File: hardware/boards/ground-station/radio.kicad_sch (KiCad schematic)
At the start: 0 parts

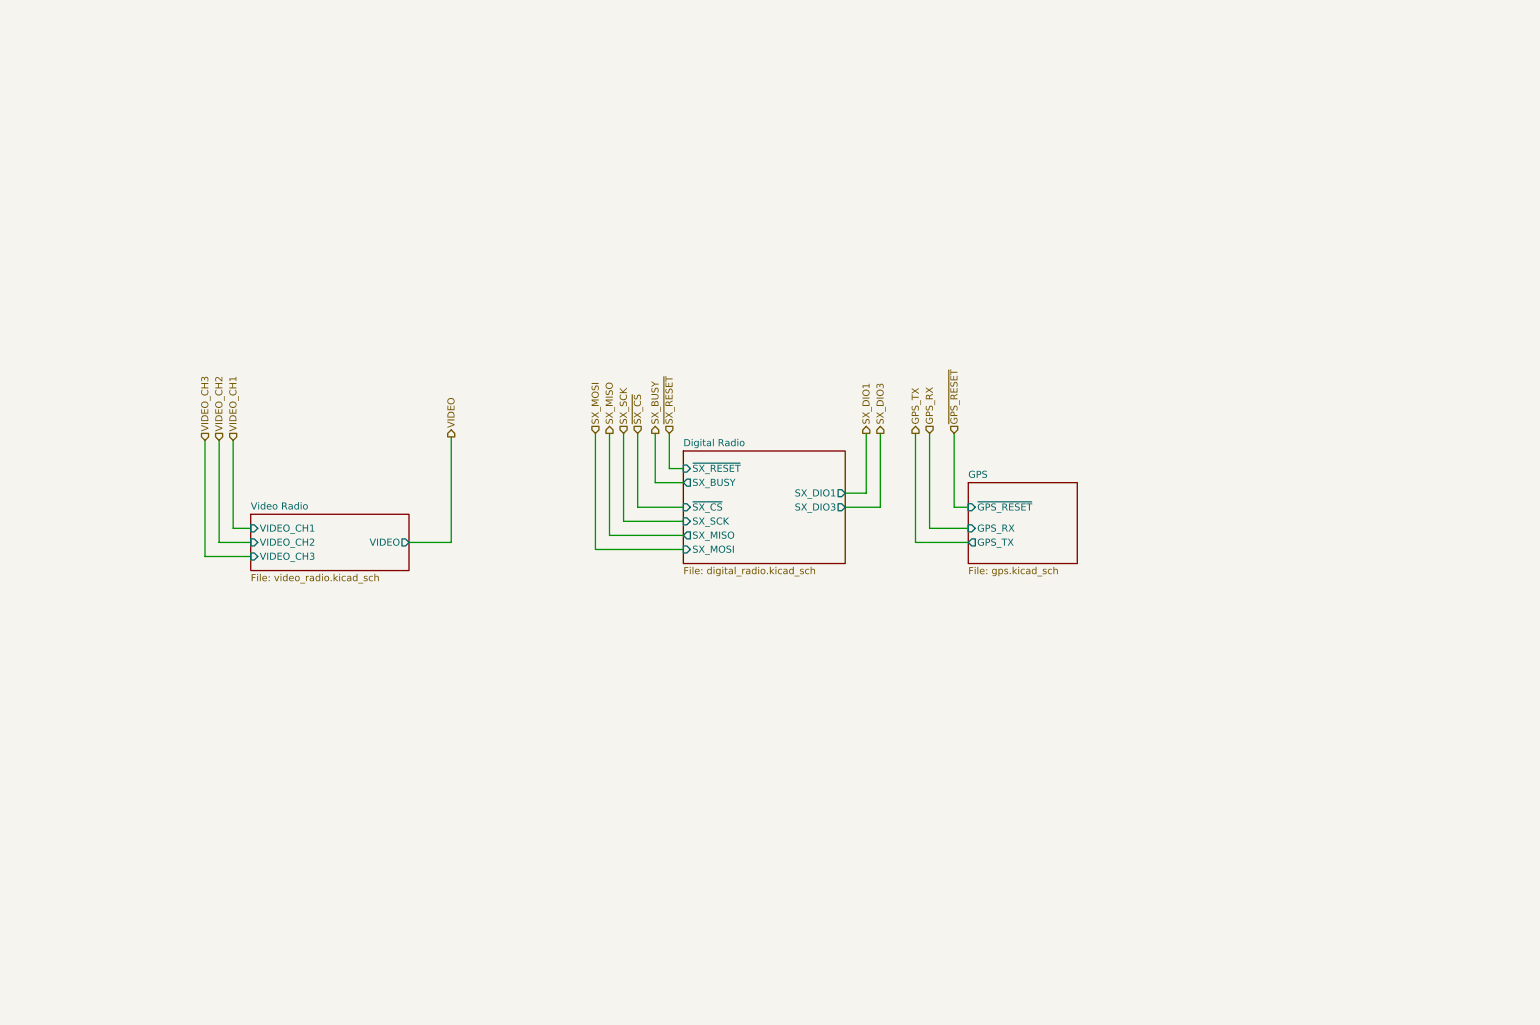
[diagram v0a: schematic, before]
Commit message: Updated video radio to RX5808
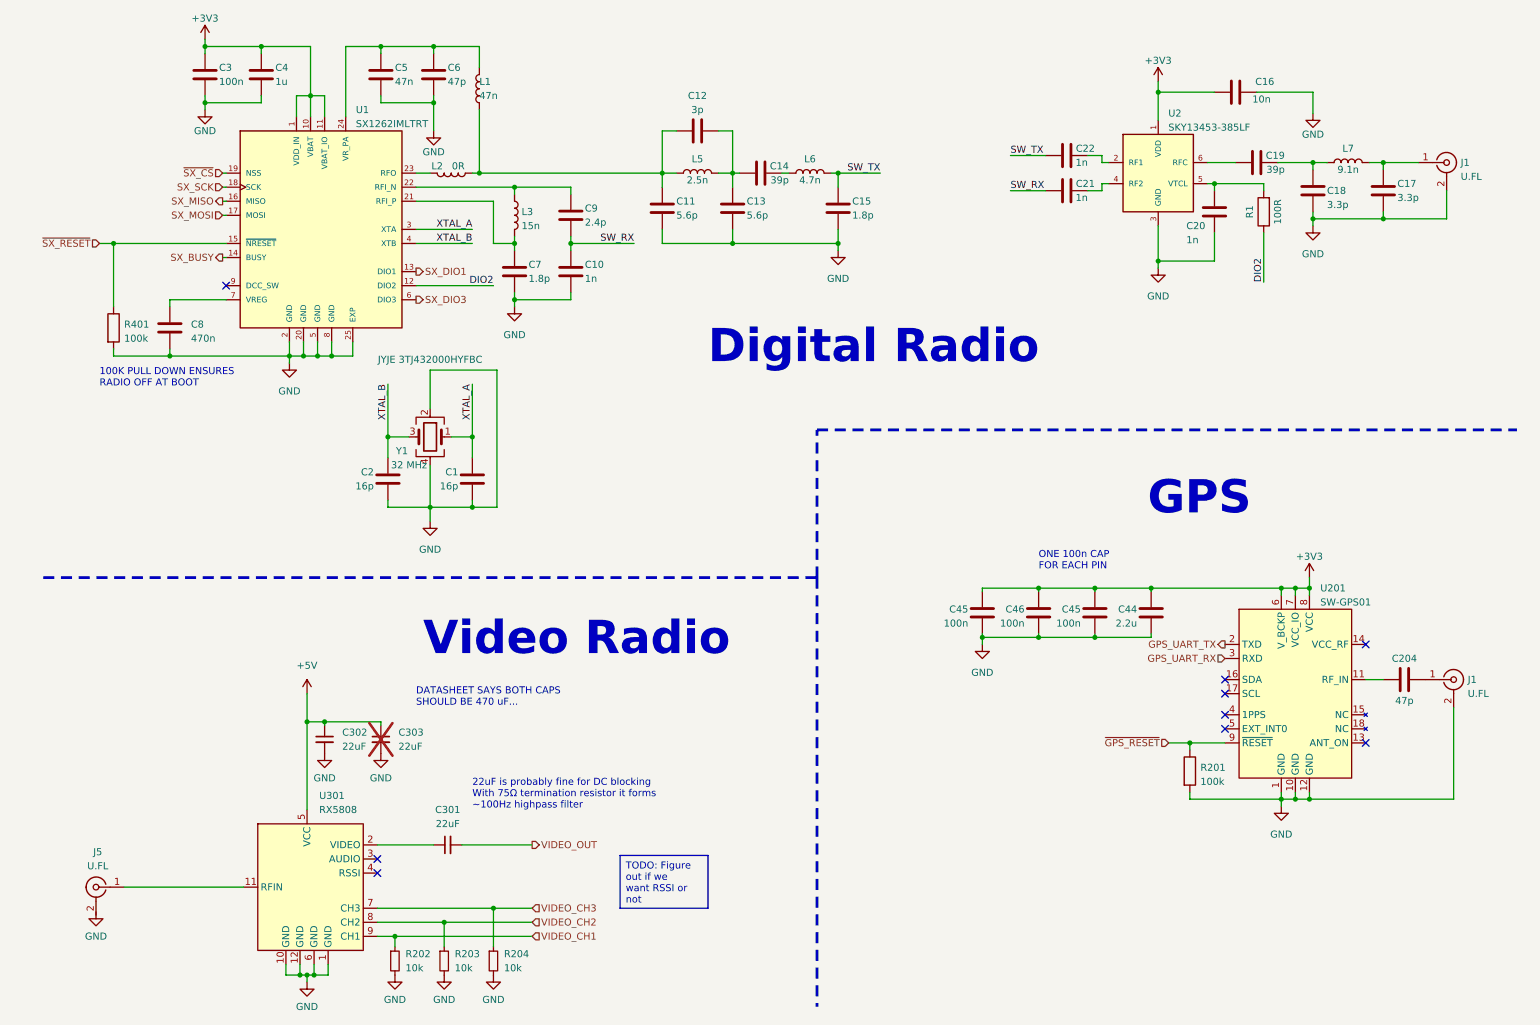
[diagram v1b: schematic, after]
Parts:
- added C1, C2: 16p, Capacitor_SMD:C_0201_0603Metric, symbol Device:C
- added C10, C21, C22: 1n, Capacitor_SMD:C_0402_1005Metric, symbol Device:C
- added C11, C13: 5.6p, Capacitor_SMD:C_0402_1005Metric, symbol Device:C
- added C12: 3p, Capacitor_SMD:C_0402_1005Metric, symbol Device:C
- added C14, C19: 39p, Capacitor_SMD:C_0402_1005Metric, symbol Device:C
- added C15, C7: 1.8p, Capacitor_SMD:C_0402_1005Metric, symbol Device:C
- added C16: 10n, Capacitor_SMD:C_0201_0603Metric, symbol Device:C
- added C17, C18: 3.3p, Capacitor_SMD:C_0402_1005Metric, symbol Device:C
- added C20: 1n, Capacitor_SMD:C_0201_0603Metric, symbol Device:C
- added C204, C6: 47p, Capacitor_SMD:C_0402_1005Metric, symbol Device:C
- added C3, C45 (x2), C46: 100n, Capacitor_SMD:C_0201_0603Metric, symbol Device:C
- added C301, C302, C303: 22uF, symbol Device:C_Small
- added C4: 1u, Capacitor_SMD:C_0402_1005Metric, symbol Device:C
- added C44: 2.2u, Capacitor_SMD:C_0402_1005Metric, symbol Device:C
- added C5: 47n, Capacitor_SMD:C_0402_1005Metric, symbol Device:C
- added C8: 470n, Capacitor_SMD:C_0402_1005Metric, symbol Device:C
- added C9: 2.4p, Capacitor_SMD:C_0402_1005Metric, symbol Device:C
- added J1 (x2), J5: U.FL, capstone:U.FL-R-SMT-1(60), symbol Connector:Conn_Coaxial
- added L1: 47n, Inductor_SMD:L_0402_1005Metric, symbol Device:L
- added L2: 0R, Inductor_SMD:L_0402_1005Metric, symbol Device:L
- added L3: 15n, Inductor_SMD:L_0402_1005Metric, symbol Device:L
- added L5: 2.5n, Inductor_SMD:L_0402_1005Metric, symbol Device:L
- added L6: 4.7n, Inductor_SMD:L_0402_1005Metric, symbol Device:L
- added L7: 9.1n, Inductor_SMD:L_0402_1005Metric, symbol Device:L
- added R1: 100R, Resistor_SMD:R_0201_0603Metric, symbol Device:R
- added R201, R401: 100k, Resistor_SMD:R_0201_0603Metric, symbol Device:R
- added R202, R203, R204: 10k, symbol Device:R_Small
- added U1: SX1262IMLTRT, capstone:SX1262IMLTRT, symbol Capstone:SX1262IMLTRT
- added U2: SKY13453-385LF, capstone:IC_SKY13453-385LF, symbol Capstone:SKY13453-385LF
- added U201: SW-GPS01, capstone:SW-GPS01, symbol Capstone:SW-GPS01
- added U301: RX5808, symbol capstone:RX5808
- added Y1: 32 MHz, capstone:JYJE-3TJ432000HYFBC, symbol Device:Crystal_GND24
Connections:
- net SX_BUSY: now also U1.14 (BUSY)
- net SX_DIO1: now also U1.13 (DIO1)
- net SX_DIO3: now also U1.6 (DIO3)
- net SX_MISO: now also U1.16 (MISO)
- net SX_MOSI: now also U1.17 (MOSI)
- net SX_SCK: now also U1.18 (SCK)
- net VIDEO_CH1: now also R202.1, U301.9 (CH1)
- net VIDEO_CH2: now also R203.1, U301.8 (CH2)
- net VIDEO_CH3: now also R204.1, U301.7 (CH3)
- net ~{GPS_RESET}: now also R201.1, U201.9 (~{RESET})
- net ~{SX_CS}: now also U1.19 (NSS)
- net ~{SX_RESET}: now also R401.1, U1.15 (~{NRESET})
- new net: C11.1, C12.1, L1.1, L2.1, L5.1
- new net: C12.2, C13.2, C14.2, L5.2
- new net: C5.1, C6.1, L1.2, U1.24 (VR_PA)
- new net: C17.2, J1.1 (In), L7.2
- new net: C8.1, U1.7 (VREG)
- new net: C18.2, C19.1, L7.1
- new net: C19.2, U2.6 (RFC)
- new net: C22.1, U2.2 (RF1)
- new net: C21.1, U2.4 (RF2)
- new net: C20.2, R1.2, U2.5 (VTCL)
- new net: C7.1, L3.2, U1.21 (RFI_P)
- new net: C9.2, L3.1, U1.22 (RFI_N)
- new net: L2.2, U1.23 (RFO)
- new net: C14.1, L6.1
- new net: C301.1, U301.2 (VIDEO)
- new net: J5.1 (In), U301.11 (RFIN)
- new net: C204.2, J1.1 (In)
- new net: C204.1, U201.11 (RF_IN)
- new net +3V3: C16.1, C3.1, C4.1, C44.1, C45.1, C45.1, C46.1, U1.1 (VDD_IN), U1.10 (VBAT), U1.11 (VBAT_IO), U2.1 (VDD), U201.6 (V_BCKP), U201.7 (VCC_IO), U201.8 (VCC)
- new net +5V: C302.1, C303.1, U301.5 (VCC)
- new net DIO2: R1.1, U1.12 (DIO2)
- new net GND: C1.2, C10.1, C11.2, C13.1, C15.1, C16.2, C17.1, C18.1, C2.2, C20.1, C3.2, C302.2, C303.2, C4.2, C44.2, C45.2, C45.2, C46.2, C5.2, C6.2, C7.2, C8.2, J1.2 (Ext), J1.2 (Ext), R201.2, R202.2, R203.2, R204.2, R401.2, U1.2 (GND), U1.20 (GND), U1.25 (EXP), U1.5 (GND), U1.8 (GND), U2.3 (GND), U201.1 (GND), U201.10 (GND), U201.12 (GND), U301.1 (GND), U301.10 (GND), U301.12 (GND), U301.6 (GND), Y1.2, Y1.4
- new net GPS_UART_RX: U201.3 (RXD)
- new net GPS_UART_TX: U201.2 (TXD)
- new net SW_RX: C10.2, C21.2, C9.1
- new net SW_TX: C15.2, C22.2, L6.2
- new net VIDEO_OUT: C301.2
- new net XTAL_A: C1.1, U1.3 (XTA), Y1.1
- new net XTAL_B: C2.1, U1.4 (XTB), Y1.3
- no-connect marks 0 -> 9
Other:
- removed sheet Digital Radio
- removed sheet GPS
- removed sheet Video Radio
- note added: "100K PULL DOWN ENSURES RADIO OFF AT BOOT"
- note added: "22uF is probably fine for DC blocking With 75Ω termination resistor it forms ~100Hz highpass filter"
- note added: "DATASHEET SAYS BOTH CAPS SHOULD BE 470 uF..."
- note added: "Digital Radio"
- note added: "GPS"
- note added: "ONE 100n CAP FOR EACH PIN"
- note added: "Video Radio"
- title: (none) -> Radios

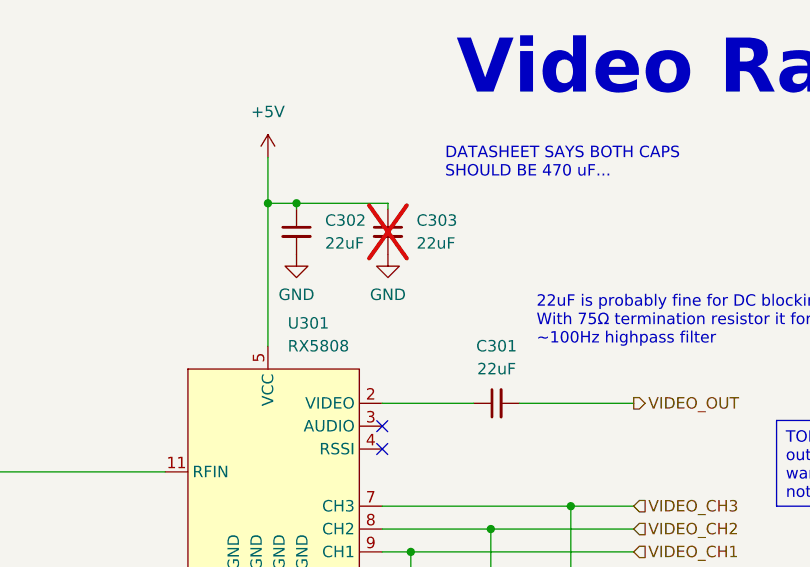
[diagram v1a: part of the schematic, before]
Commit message: Transmitting power (without wires) (wire delete)
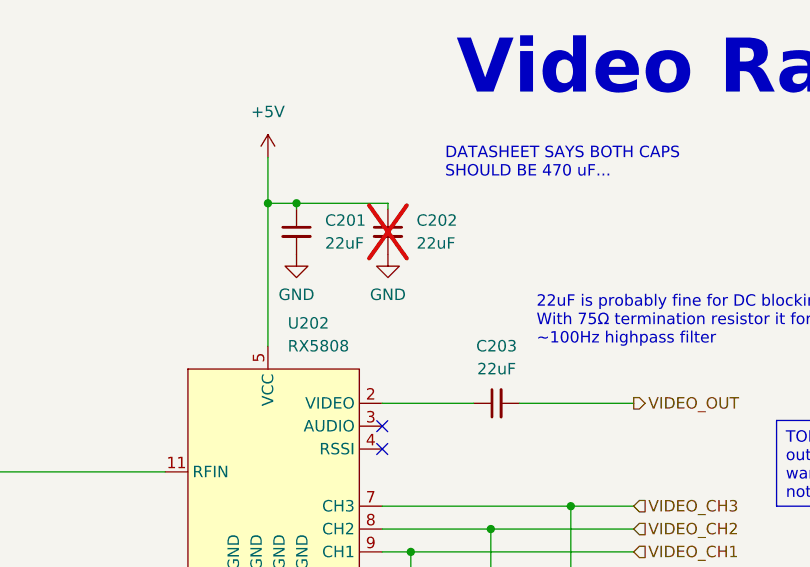
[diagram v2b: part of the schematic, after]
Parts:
- renumbered C302 to C201, C303 to C202, C301 to C203, U301 to U202
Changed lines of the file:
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@@
   (symbol (lib_id "power:GND") (at 76.835 148.59 0) (unit 1)
     (in_bom yes) (on_board yes) (dnp no)
-    (property "Reference" "#PWR0308" (at 76.835 154.94 0)
+    (property "Reference" "#PWR0207" (at 76.835 154.94 0)
       (effects (font (size 1.27 1.27)) hide)
     )
@@
   (symbol (lib_id "Device:C_Small") (at 76.835 146.05 0) (unit 1)
     (in_bom yes) (on_board yes) (dnp yes) (fields_autoplaced)
-    (property "Reference" "C303" (at 80.01 144.7863 0)
+    (property "Reference" "C202" (at 80.01 144.7863 0)
       (effects (font (size 1.27 1.27)) (justify left))
     )
@@
   (symbol (lib_id "power:GND") (at 25.4 177.165 0) (unit 1)
     (in_bom yes) (on_board yes) (dnp no) (fields_autoplaced)
-    (property "Reference" "#PWR0301" (at 25.4 183.515 0)
+    (property "Reference" "#PWR0202" (at 25.4 183.515 0)
       (effects (font (size 1.27 1.27)) hide)
     )
@@
   (symbol (lib_id "power:+5V") (at 63.5 137.795 0) (unit 1)
     (in_bom yes) (on_board yes) (dnp no) (fields_autoplaced)
-    (property "Reference" "#PWR0306" (at 63.5 141.605 0)
+    (property "Reference" "#PWR0204" (at 63.5 141.605 0)
       (effects (font (size 1.27 1.27)) hide)
     )
@@
   (symbol (lib_id "power:GND") (at 79.375 188.595 0) (unit 1)
     (in_bom yes) (on_board yes) (dnp no) (fields_autoplaced)
-    (property "Reference" "#PWR0303" (at 79.375 194.945 0)
+    (property "Reference" "#PWR0208" (at 79.375 194.945 0)
       (effects (font (size 1.27 1.27)) hide)
     )
@@
   (symbol (lib_id "Device:C_Small") (at 88.9 165.1 90) (unit 1)
     (in_bom yes) (on_board yes) (dnp no) (fields_autoplaced)
-    (property "Reference" "C301" (at 88.9063 158.75 90)
+    (property "Reference" "C203" (at 88.9063 158.75 90)
       (effects (font (size 1.27 1.27)))
     )
@@
   (symbol (lib_id "power:GND") (at 63.5 189.865 0) (unit 1)
     (in_bom yes) (on_board yes) (dnp no) (fields_autoplaced)
-    (property "Reference" "#PWR0302" (at 63.5 196.215 0)
+    (property "Reference" "#PWR0205" (at 63.5 196.215 0)
       (effects (font (size 1.27 1.27)) hide)
     )
@@
   (symbol (lib_id "power:GND") (at 97.155 188.595 0) (unit 1)
     (in_bom yes) (on_board yes) (dnp no) (fields_autoplaced)
-    (property "Reference" "#PWR0305" (at 97.155 194.945 0)
+    (property "Reference" "#PWR0210" (at 97.155 194.945 0)
       (effects (font (size 1.27 1.27)) hide)
     )
@@
   (symbol (lib_id "power:GND") (at 88.265 188.595 0) (unit 1)
     (in_bom yes) (on_board yes) (dnp no) (fields_autoplaced)
-    (property "Reference" "#PWR0304" (at 88.265 194.945 0)
+    (property "Reference" "#PWR0209" (at 88.265 194.945 0)
       (effects (font (size 1.27 1.27)) hide)
     )
@@
   (symbol (lib_id "capstone:RX5808") (at 63.5 172.72 0) (unit 1)
     (in_bom yes) (on_board yes) (dnp no) (fields_autoplaced)
-    (property "Reference" "U301" (at 65.6941 156.21 0)
+    (property "Reference" "U202" (at 65.6941 156.21 0)
       (effects (font (size 1.27 1.27)) (justify left))
     )
@@
   (symbol (lib_id "power:GND") (at 66.675 148.59 0) (unit 1)
     (in_bom yes) (on_board yes) (dnp no)
-    (property "Reference" "#PWR0307" (at 66.675 154.94 0)
+    (property "Reference" "#PWR0206" (at 66.675 154.94 0)
       (effects (font (size 1.27 1.27)) hide)
     )
@@
   (symbol (lib_id "Device:C_Small") (at 66.675 146.05 0) (unit 1)
     (in_bom yes) (on_board yes) (dnp no) (fields_autoplaced)
-    (property "Reference" "C302" (at 69.85 144.7863 0)
-      (effects (font (size 1.27 1.27)) (justify left))
-    )
+    (property "Reference" "C201" (at 69.85 144.7863 0)
+      (effects (font (size 1.27 1.27)) (justify left))
+    )

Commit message: sch review
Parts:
- added J3: Conn_Coaxial, symbol Connector:Conn_Coaxial
- added TP1, TP2: TestPoint, symbol Connector:TestPoint
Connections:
- net GND: now also J3.2 (Ext)
- net VIDEO_OUT: now also J3.1 (In)
- net at U202.3 (AUDIO): now also TP2.1
- net at U202.4 (RSSI): now also TP1.1
- no-connect marks 9 -> 7
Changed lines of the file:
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@@
   (junction (at 257.81 52.07) (diameter 0) (color 0 0 0 0)
   )
+  (junction (at 100.33 165.1) (diameter 0) (color 0 0 0 0)
+  )
   (junction (at 66.675 142.875) (diameter 0) (color 0 0 0 0)
   )
@@
   (no_connect (at 229.235 135.255))
   (no_connect (at 48.895 64.135))
-  (no_connect (at 76.2 170.18))
   (no_connect (at 229.235 144.145))
-  (no_connect (at 76.2 167.64))
   (no_connect (at 229.235 141.605))
   (wire (pts (xy 93.345 102.87) (xy 93.345 104.14))
@@
     (stroke (width 0) (type default))
   )
+  (wire (pts (xy 76.2 170.18) (xy 77.47 170.18))
+    (stroke (width 0) (type default))
+  )
   (wire (pts (xy 93.345 91.44) (xy 93.345 95.25))
     (stroke (width 0) (type default))
@@
     (stroke (width 0) (type default))
   )
-  (wire (pts (xy 104.14 165.1) (xy 91.44 165.1))
+  (wire (pts (xy 104.14 165.1) (xy 100.33 165.1))
     (stroke (width 0) (type default))
   )
@@
     (stroke (width 0) (type default))
   )
+  (wire (pts (xy 76.2 167.64) (xy 77.47 167.64))
+    (stroke (width 0) (type default))
+  )
   (wire (pts (xy 59.69 186.69) (xy 59.69 188.595))
     (stroke (width 0) (type default))
   )
+  (wire (pts (xy 118.11 161.29) (xy 100.33 161.29))
+    (stroke (width 0) (type default))
+  )
   (wire (pts (xy 204.47 46.99) (xy 207.01 46.99))
     (stroke (width 0) (type default))
@@
     (stroke (width 0) (type default))
   )
+  (wire (pts (xy 100.33 165.1) (xy 91.44 165.1))
+    (stroke (width 0) (type default))
+  )
   (wire (pts (xy 140.335 36.195) (xy 140.335 43.815))
     (stroke (width 0) (type default))
@@
     (stroke (width 0) (type default))
   )
+  (wire (pts (xy 123.19 166.37) (xy 123.19 167.005))
+    (stroke (width 0) (type default))
+  )
   (wire (pts (xy 195.58 127.635) (xy 205.74 127.635))
     (stroke (width 0) (type default))
@@
     (stroke (width 0) (type default))
   )
+  (wire (pts (xy 100.33 161.29) (xy 100.33 165.1))
+    (stroke (width 0) (type default))
+  )
   (wire (pts (xy 254.635 135.255) (xy 257.81 135.255))
     (stroke (width 0) (type default))
@@
   )
   (text_box "TODO: Figure out if we want RSSI or not"
-    (at 120.015 167.005 0) (size 15.875 9.525)
+    (at 120.015 175.895 0) (size 15.875 9.525)
     (stroke (width 0) (type default))
     (fill (type color) (color 255 255 0 1))
@@
   )
   (text "22uF is probably fine for DC blocking\nWith 75Ω termination resistor it forms\n~100Hz highpass filter"
-    (at 93.345 158.75 0)
+    (at 93.345 156.21 0)
     (effects (font (size 1.27 1.27)) (justify left bottom))
   )
@@
     )
   )
+  (symbol (lib_id "power:GND") (at 123.19 167.005 0) (unit 1)
+    (in_bom yes) (on_board yes) (dnp no)
+    (property "Reference" "#PWR05" (at 123.19 173.355 0)
+      (effects (font (size 1.27 1.27)) hide)
+    )
+    (property "Value" "GND" (at 123.19 170.815 0)
+      (effects (font (size 1.27 1.27)))
+    )
+    (property "Footprint" "" (at 123.19 167.005 0)
+      (effects (font (size 1.27 1.27)) hide)
+    )
+    (property "Datasheet" "" (at 123.19 167.005 0)
+      (effects (font (size 1.27 1.27)) hide)
+    )
+    (pin "1")
+    (instances
+      (project "ground-station"
+        (path "/ce329892-de08-4d39-b253-15f3aaf1c085/37a6bbaf-9821-4b58-bc66-fc0453299811"
+          (reference "#PWR05") (unit 1)
+        )
+      )
+    )
+  )
   (symbol (lib_id "Device:C") (at 205.74 123.19 0) (mirror y) (unit 1)
     (in_bom yes) (on_board yes) (dnp no)
@@
     )
   )
+  (symbol (lib_id "Connector:TestPoint") (at 77.47 167.64 270) (unit 1)
+    (in_bom yes) (on_board yes) (dnp no)
+    (property "Reference" "TP2" (at 81.915 167.64 90)
+      (effects (font (size 1.27 1.27)) (justify left))
+    )
+    (property "Value" "TestPoint" (at 82.55 169.545 90)
+      (effects (font (size 1.27 1.27)) (justify left) hide)
+    )
+    (property "Footprint" "" (at 77.47 172.72 0)
+      (effects (font (size 1.27 1.27)) hide)
+    )
+    (property "Datasheet" "~" (at 77.47 172.72 0)
+      (effects (font (size 1.27 1.27)) hide)
+    )
+    (pin "1")
+    (instances
+      (project "ground-station"
+        (path "/ce329892-de08-4d39-b253-15f3aaf1c085/37a6bbaf-9821-4b58-bc66-fc0453299811"
+          (reference "TP2") (unit 1)
+        )
+      )
+    )
+  )
   (symbol (lib_id "power:GND") (at 79.375 188.595 0) (unit 1)
     (in_bom yes) (on_board yes) (dnp no) (fields_autoplaced)
@@
     )
   )
+  (symbol (lib_id "Connector:TestPoint") (at 77.47 170.18 270) (unit 1)
+    (in_bom yes) (on_board yes) (dnp no)
+    (property "Reference" "TP1" (at 81.915 170.18 90)
+      (effects (font (size 1.27 1.27)) (justify left))
+    )
+    (property "Value" "TestPoint" (at 82.55 172.085 90)
+      (effects (font (size 1.27 1.27)) (justify left) hide)
+    )
+    (property "Footprint" "" (at 77.47 175.26 0)
+      (effects (font (size 1.27 1.27)) hide)
+    )
+    (property "Datasheet" "~" (at 77.47 175.26 0)
+      (effects (font (size 1.27 1.27)) hide)
+    )
+    (pin "1")
+    (instances
+      (project "ground-station"
+        (path "/ce329892-de08-4d39-b253-15f3aaf1c085/37a6bbaf-9821-4b58-bc66-fc0453299811"
+          (reference "TP1") (unit 1)
+        )
+      )
+    )
+  )
   (symbol (lib_id "Device:C") (at 145.415 43.815 270) (unit 1)
     (in_bom yes) (on_board yes) (dnp no)
@@
         )
       )
+    )
+  )
+  (symbol (lib_id "Connector:Conn_Coaxial") (at 123.19 161.29 0) (unit 1)
+    (in_bom yes) (on_board yes) (dnp no) (fields_autoplaced)
+    (property "Reference" "J3" (at 126.365 160.3132 0)
+      (effects (font (size 1.27 1.27)) (justify left))
+    )
+    (property "Value" "Conn_Coaxial" (at 126.365 162.8532 0)
+      (effects (font (size 1.27 1.27)) (justify left))
+    )
+    (property "Footprint" "" (at 123.19 161.29 0)
+      (effects (font (size 1.27 1.27)) hide)
+    )
+    (property "Datasheet" " ~" (at 123.19 161.29 0)
+      (effects (font (size 1.27 1.27)) hide)
+    )
+    (pin "2")
+    (pin "1")
+    (instances
+      (project "ground-station"
+        (path "/ce329892-de08-4d39-b253-15f3aaf1c085/37a6bbaf-9821-4b58-bc66-fc0453299811"
+          (reference "J3") (unit 1)
+        )
+      )
